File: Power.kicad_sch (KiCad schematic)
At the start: 30 parts, among them U10 RT8259GJ6, U9 LMR14050SDDA

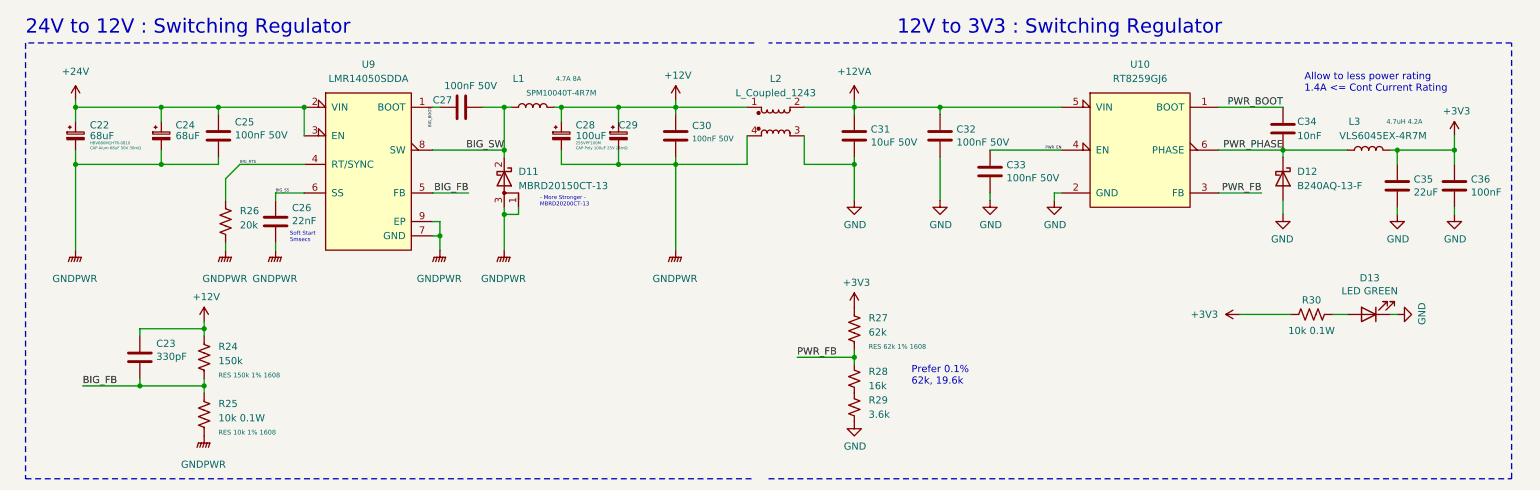
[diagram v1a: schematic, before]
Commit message: some layout changed (sizeup for later 2layer conversion)
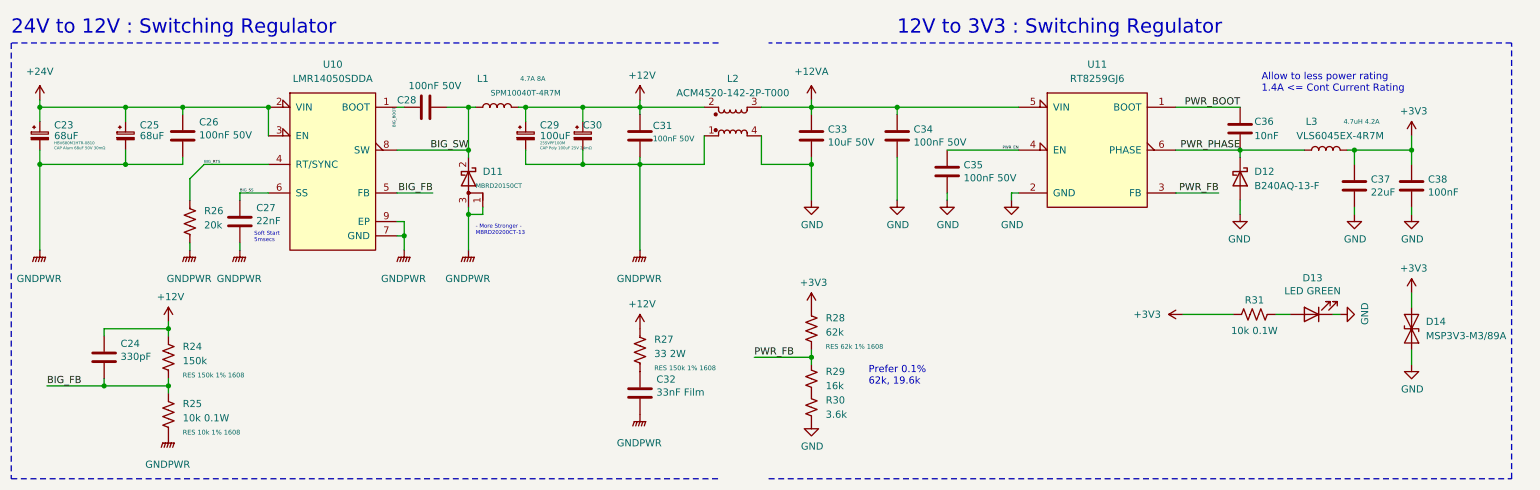
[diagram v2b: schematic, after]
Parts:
- added C32: 33nF Film, Capacitor_SMD:C_1210_3225Metric, symbol Device:C
- added D14: MSP3V3-M3/89A, Diode_SMD:D_SMF, symbol Diode:SD36_SOD323
- added R27: 33 2W, Resistor_SMD:R_2512_6332Metric, symbol Device:R_US
- D11: value MBRD20150CT-13 -> MBRD20150CT
- L2: value L_Coupled_1243 -> ACM4520-142-2P-T000; symbol Device:L_Coupled_1243 -> Device:L_Coupled_1423
- renumbered C22 to C23, C23 to C24, C24 to C25, C25 to C26, C26 to C27, C27 to C28, C28 to C29, C29 to C30, C30 to C31, C31 to C33, C32 to C34, C33 to C35, C34 to C36, C35 to C37, C36 to C38, R27 to R28, R28 to R29, R29 to R30, R30 to R31, U9 to U10, U10 to U11
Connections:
- net +12V: now also L2.2, R27.1; no longer L2.1
- net +12VA: now also L2.3; no longer L2.2
- net +3V3: now also D14.2 (A2)
- net GND: now also L2.4, D14.1 (A1); no longer L2.3
- net GNDPWR: now also L2.1, C32.2; no longer L2.4
- new net: C32.1, R27.2
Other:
- moved on the sheet: C23, C24, C25, C26, C27, C28, C29, C30, C31, C33, C34, C35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
